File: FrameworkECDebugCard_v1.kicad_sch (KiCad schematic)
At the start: 29 parts, among them J1 Conn_01x05, P1 1054440011, P2 2169900001, U1 FT230XS

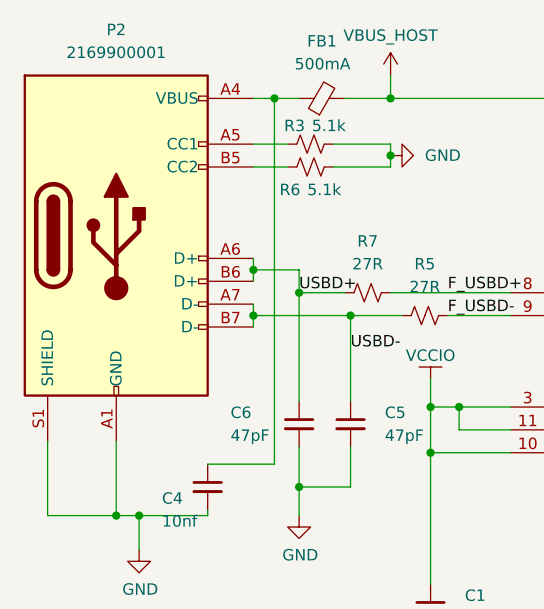
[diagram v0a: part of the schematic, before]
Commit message: Exclude P2 from PCBWay/JLCPCB assembly (cheaper to do it manually)
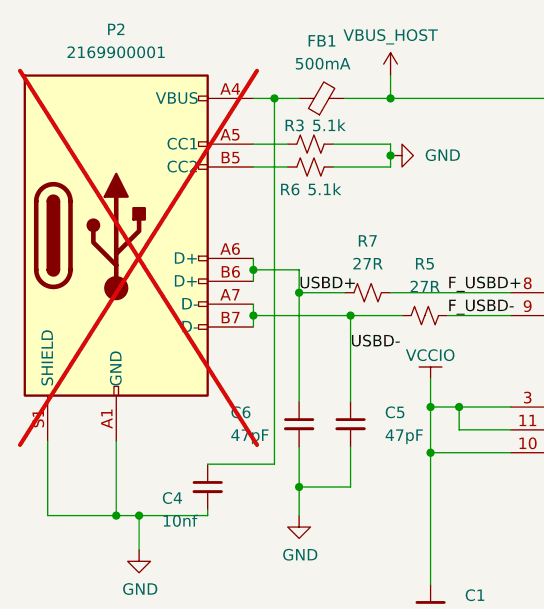
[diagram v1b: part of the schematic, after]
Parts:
- P2: now not fitted; now left out of the parts list
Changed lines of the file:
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@@
 		(unit 1)
 		(exclude_from_sim no)
-		(in_bom yes)
+		(in_bom no)
 		(on_board yes)
-		(dnp no)
+		(dnp yes)
 		(fields_autoplaced yes)
 		(property "Reference" "P2"
